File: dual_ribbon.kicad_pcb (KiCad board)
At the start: 2 copper layers, 53 parts, among them J1 Conn_01x02_Socket, J2 Conn_01x02_Socket, J3 Conn_01x02_Socket, J4 Conn_01x02_Socket, Q1 PNP, Q2 MMBF4391, Q3 MMBF4391, U1 LM4041LP-ADJ, U2 TL072, U3 OPA2134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

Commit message: Layout mostly finished
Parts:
- added U5: TL072, Package_SO:SOIC-8_3.9x4.9mm_P1.27mm, F.Cu at (148.0, 101.0)
- U2: footprint Package_SO:SOIC-10_3.9x4.9mm_P1mm -> Package_SO:SOIC-8_3.9x4.9mm_P1.27mm
- U4: value TL074 -> TL072; footprint Package_SO:SOIC-14_3.9x8.7mm_P1.27mm -> Package_SO:SOIC-8_3.9x4.9mm_P1.27mm
- moved TRIM1 82.9 mm to (148.7, 126.0)
- moved J2 78.4 mm to (113.1, 99.5)
- moved LEVEL1 77.0 mm to (113.2, 104.5)
- moved R1 76.5 mm to (144.9, 127.0)
- moved J3 72.6 mm to (118.5, 116.6), turned to -90 degrees
- moved Q1 66.4 mm to (153.9, 108.0)
- moved RANGE1 66.2 mm to (148.7, 122.0)
- moved C7 62.2 mm to (161.0, 116.0), turned to 180 degrees
- moved J1 61.4 mm to (122.5, 116.6), turned to -90 degrees
- moved RIBBON1 60.4 mm to (139.9, 95.0)
- moved U1 57.8 mm to (155.0, 112.0), turned to 180 degrees
- moved R18 53.6 mm to (121.6, 109.5), turned to 180 degrees
- moved R15 53.1 mm to (118.0, 109.5)
- moved U2 52.1 mm to (126.4, 110.5), turned to 90 degrees
- moved R8 51.7 mm to (149.5, 116.4), turned to -90 degrees
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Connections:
- C3 pad 2: Net-(U4A--) -> Net-(U4B--)
- C4 pad 1: Net-(U4B--) -> Net-(U4A--)
- R3 pad 1: Net-(U4C-+) -> Net-(U5A-+)
- R4 pad 1: Net-(U4C-+) -> Net-(U5A-+)
- R5 pad 1: Net-(U4A--) -> Net-(U4B--)
- R6 pad 1: Net-(U4B--) -> Net-(U4A--)
- R7 pad 2: Net-(U4A--) -> Net-(U4B--)
- R8 pad 2: Net-(U4B--) -> Net-(U4A--)
- U4 pad 1: Net-(Q3-D) -> Net-(Q2-D)
- U4 pad 4: +12V -> -12V
- U4 pad 7: Net-(Q2-D) -> Net-(Q3-D)
- U4 pad 8: Net-(D2-K) -> +12V
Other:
- board outline added: 100.5 x 101 mm

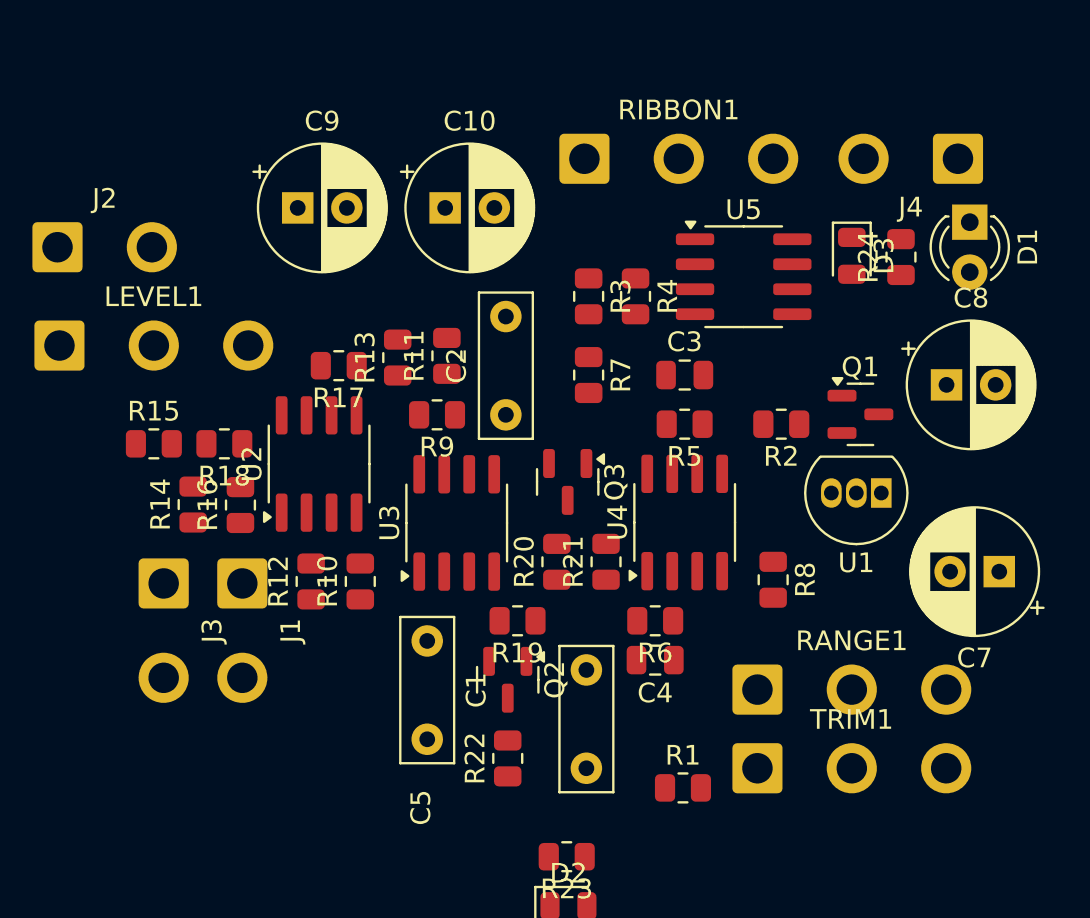
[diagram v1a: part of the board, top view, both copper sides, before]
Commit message: Did most of the routing
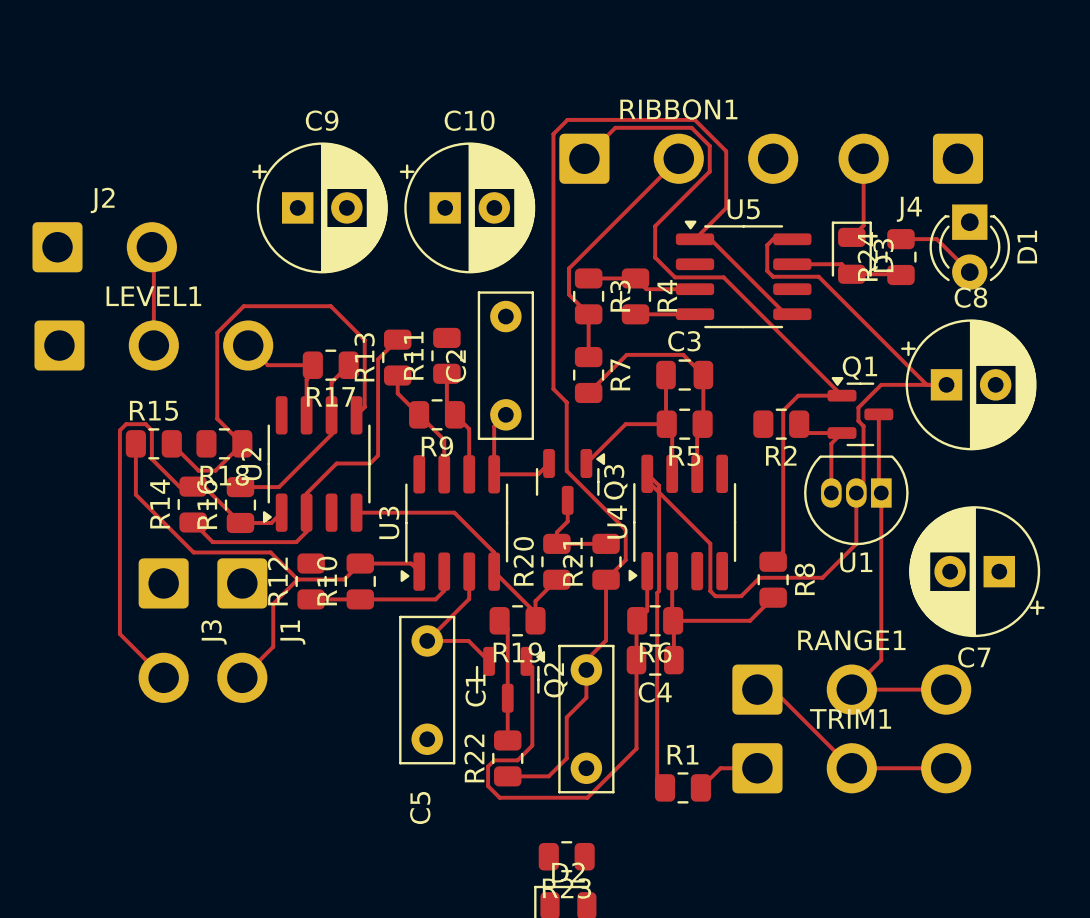
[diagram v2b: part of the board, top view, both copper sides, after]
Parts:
- moved R17 0.41 mm to (127.0, 105.5)
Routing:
- net Net-(D2-K): track 0.00 -> 59.3 mm
- net +12V: track 0.00 -> 58.7 mm
- net Net-(Q1-C): track 0.00 -> 37.8 mm
- net Net-(Q2-D): track 0.00 -> 26.2 mm
- net Net-(J1-Pin_2): track 0.00 -> 25.5 mm
- net Net-(J3-Pin_2): track 0.00 -> 25.0 mm
- net Net-(U2B-+): track 0.00 -> 23.7 mm
- net Net-(Q1-E): track 0.00 -> 19.5 mm
- net Net-(U2A--): track 0.00 -> 19.1 mm
- net -12V: track 0.00 -> 17.8 mm
- net Net-(R3-Pad2): track 0.00 -> 12.8 mm
- net Net-(U4B--): track 0.00 -> 12.2 mm
- net Net-(RANGE1-Pad1): track 0.00 -> 11.3 mm
- net Net-(U4A--): track 0.00 -> 10.1 mm
- net Net-(Q3-D): track 0.00 -> 10.1 mm
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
